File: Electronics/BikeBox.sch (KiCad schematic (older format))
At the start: 0 parts

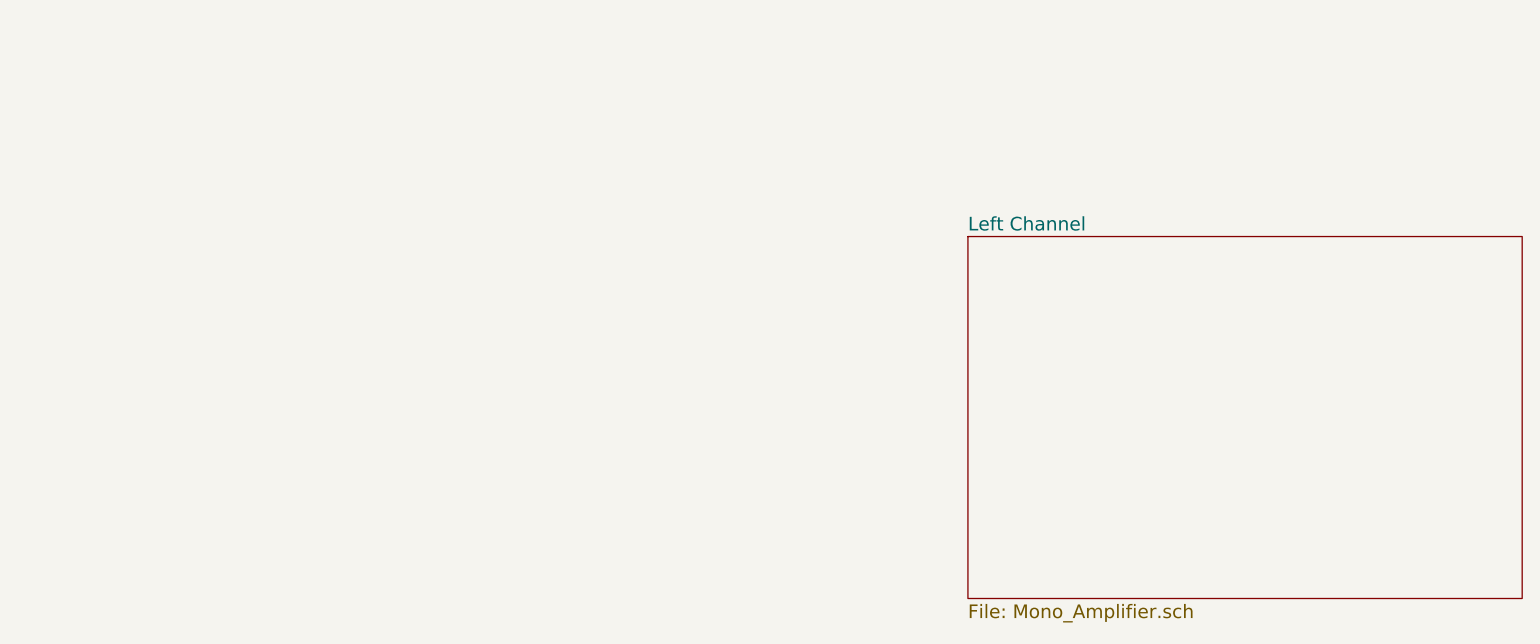
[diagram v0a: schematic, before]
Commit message: Added a few connectors Cleaning up some of the labels
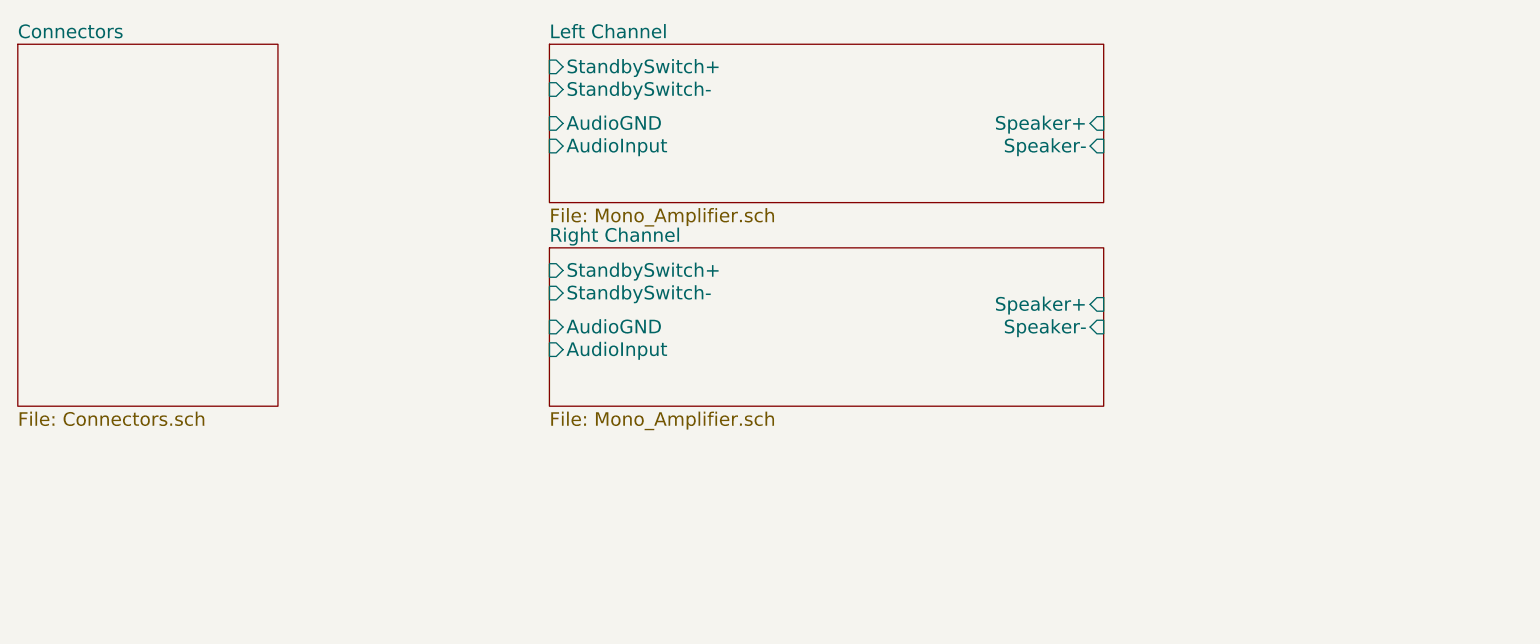
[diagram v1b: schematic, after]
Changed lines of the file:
@@
-EESchema Schematic File Version 2  date 8/2/2012 12:00:58 PM
+EESchema Schematic File Version 2  date 8/2/2012 3:30:21 PM
 LIBS:power
 LIBS:device
@@
 $Descr A4 11700 8267
 encoding utf-8
-Sheet 1 2
+Sheet 1 4
 Title ""
 Date "2 aug 2012"
@@
 $EndDescr
 $Sheet
-S 7700 1950 2450 1600
+S 3500 1100 1150 1600
+U 501ABD40
+F0 "Connectors" 60
+F1 "Connectors.sch" 60
+$EndSheet
+$Sheet
+S 5850 2000 2450 700
+U 501ABAFF
+F0 "Right Channel" 60
+F1 "Mono_Amplifier.sch" 60
+F2 "AudioGND" I L 5850 2350 60
+F3 "AudioInput" I L 5850 2450 60
+F4 "Speaker-" I R 8300 2350 60
+F5 "Speaker+" I R 8300 2250 60
+F6 "StandbySwitch-" I L 5850 2200 60
+F7 "StandbySwitch+" I L 5850 2100 60
+$EndSheet
+$Sheet
+S 5850 1100 2450 700
 U 501AA789
 F0 "Left Channel" 60
 F1 "Mono_Amplifier.sch" 60
+F2 "AudioGND" I L 5850 1450 60
+F3 "AudioInput" I L 5850 1550 60
+F4 "Speaker-" I R 8300 1550 60
+F5 "Speaker+" I R 8300 1450 60
+F6 "StandbySwitch-" I L 5850 1300 60
+F7 "StandbySwitch+" I L 5850 1200 60
 $EndSheet
 $EndSCHEMATC

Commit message: I think the first draft is done. Next step is to get a rough PCB setup.
Still need to find componets for all of the
caps, resistors, fuse, and connectors
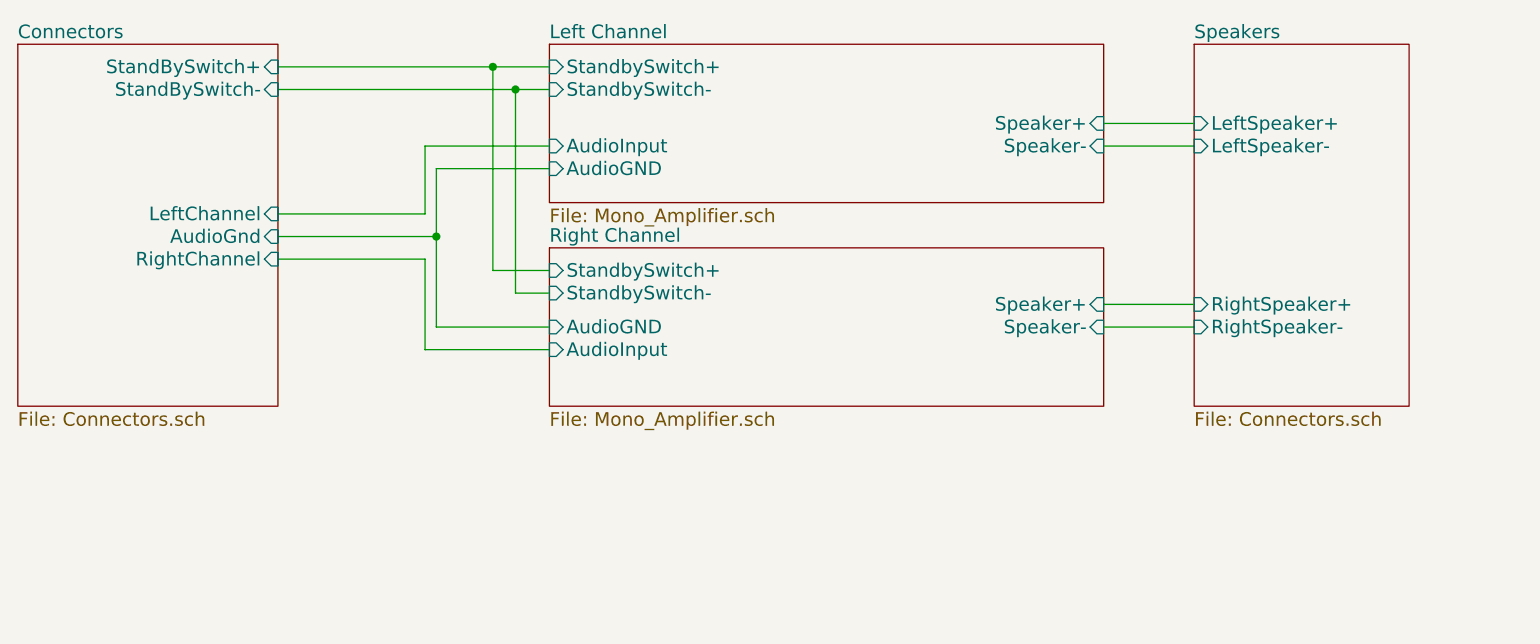
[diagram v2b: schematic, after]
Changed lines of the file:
@@
-EESchema Schematic File Version 2  date 8/2/2012 3:30:21 PM
+EESchema Schematic File Version 2  date 8/2/2012 4:04:56 PM
 LIBS:power
 LIBS:device
@@
 $Descr A4 11700 8267
 encoding utf-8
-Sheet 1 4
+Sheet 1 5
 Title ""
 Date "2 aug 2012"
@@
 Comment4 ""
 $EndDescr
+Wire Wire Line
+	8300 2350 8700 2350
+Wire Wire Line
+	8300 1550 8700 1550
+Connection ~ 5700 1300
+Connection ~ 5600 1200
+Wire Wire Line
+	5600 1200 5600 2100
+Wire Wire Line
+	5600 2100 5850 2100
+Wire Wire Line
+	5850 2450 5300 2450
+Wire Wire Line
+	5300 2450 5300 2050
+Wire Wire Line
+	5300 2050 4650 2050
+Wire Wire Line
+	5850 1650 5350 1650
+Wire Wire Line
+	5350 1950 4650 1950
+Wire Wire Line
+	4650 1850 5300 1850
+Wire Wire Line
+	5300 1850 5300 1550
+Wire Wire Line
+	5300 1550 5850 1550
+Wire Wire Line
+	5350 1650 5350 2350
+Wire Wire Line
+	5350 2350 5850 2350
+Connection ~ 5350 1950
+Wire Wire Line
+	5850 2200 5700 2200
+Wire Wire Line
+	5700 2200 5700 1300
+Wire Wire Line
+	4650 1200 5850 1200
+Wire Wire Line
+	4650 1300 5850 1300
+Wire Wire Line
+	8300 1450 8700 1450
+Wire Wire Line
+	8300 2250 8700 2250
+$Sheet
+S 8700 1100 950  1600
+U 501AEA19
+F0 "Speakers" 60
+F1 "Connectors.sch" 60
+F2 "RightSpeaker-" I L 8700 2350 60
+F3 "RightSpeaker+" I L 8700 2250 60
+F4 "LeftSpeaker-" I L 8700 1550 60
+F5 "LeftSpeaker+" I L 8700 1450 60
+$EndSheet
 $Sheet
 S 3500 1100 1150 1600
@@
 F0 "Connectors" 60
 F1 "Connectors.sch" 60
+F2 "LeftChannel" I R 4650 1850 60
+F3 "AudioGnd" I R 4650 1950 60
+F4 "RightChannel" I R 4650 2050 60
+F5 "StandBySwitch+" I R 4650 1200 60
+F6 "StandBySwitch-" I R 4650 1300 60
 $EndSheet
 $Sheet
@@
 F0 "Left Channel" 60
 F1 "Mono_Amplifier.sch" 60
-F2 "AudioGND" I L 5850 1450 60
+F2 "AudioGND" I L 5850 1650 60
 F3 "AudioInput" I L 5850 1550 60
 F4 "Speaker-" I R 8300 1550 60
